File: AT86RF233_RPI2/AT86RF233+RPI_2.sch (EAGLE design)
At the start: 10 parts, among them SW1 KSR2XYG, U1 ATZB-RF-233-1-C

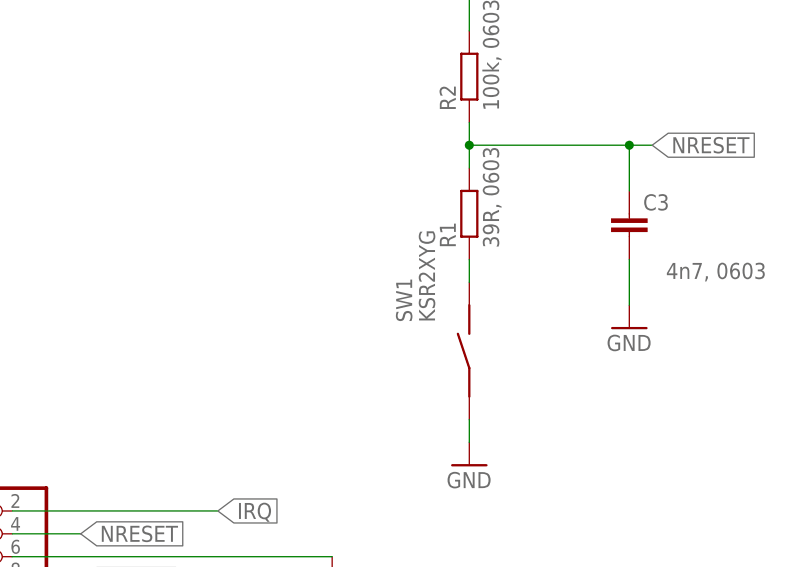
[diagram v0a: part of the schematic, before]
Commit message: at86rf233: SW1 renamed to RESET & minor alignemt improvements.
Signed-off-by: malo <malo@25cmsquare.io>
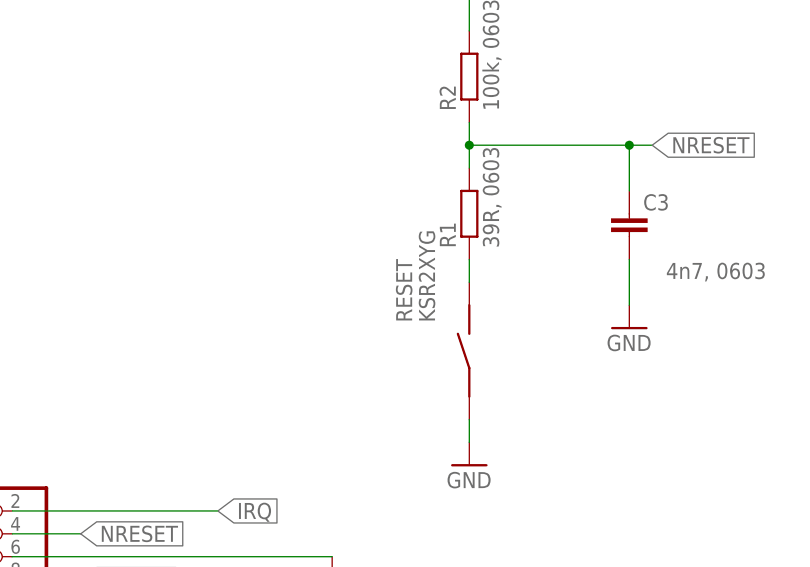
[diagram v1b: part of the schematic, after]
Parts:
- renumbered SW1 to RESET
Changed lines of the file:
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@@
 <part name="C3" library="rcl" deviceset="C-EU" device="C0603K" value="4n7, 0603"/>
 <part name="GND7" library="supply1" deviceset="GND" device=""/>
-<part name="SW1" library="25cmsquare" deviceset="KSR2XYG" device=""/>
+<part name="RESET" library="25cmsquare" deviceset="KSR2XYG" device=""/>
 </parts>
 <sheets>
@@
 </instance>
 <instance part="GND7" gate="1" x="223.52" y="119.38"/>
-<instance part="SW1" gate="G$1" x="205.74" y="116.84"/>
+<instance part="RESET" gate="G$1" x="205.74" y="116.84"/>
 </instances>
 <busses>
@@
 <pinref part="GND6" gate="1" pin="GND"/>
 <wire x1="205.74" y1="106.68" x2="205.74" y2="109.22" width="0.1524" layer="91"/>
-<pinref part="SW1" gate="G$1" pin="2"/>
+<pinref part="RESET" gate="G$1" pin="2"/>
 </segment>
 <segment>
@@
 <pinref part="R1" gate="G$1" pin="1"/>
 <wire x1="205.74" y1="124.46" x2="205.74" y2="127" width="0.1524" layer="91"/>
-<pinref part="SW1" gate="G$1" pin="1"/>
-</segment>
-</net>
+<pinref part="RESET" gate="G$1" pin="1"/>
+</segment>
+</net>
